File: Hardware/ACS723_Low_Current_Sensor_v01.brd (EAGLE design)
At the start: 31.8 x 15.2 mm, 26 parts, among them U1 ACS723, U2 OPA344

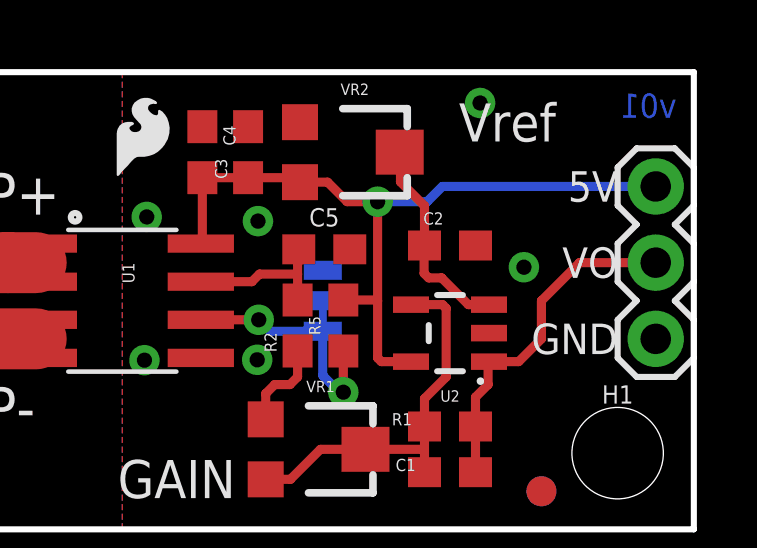
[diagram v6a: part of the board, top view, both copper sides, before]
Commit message: Adjusted the position of a cap
-C2  Y-axis -.05"
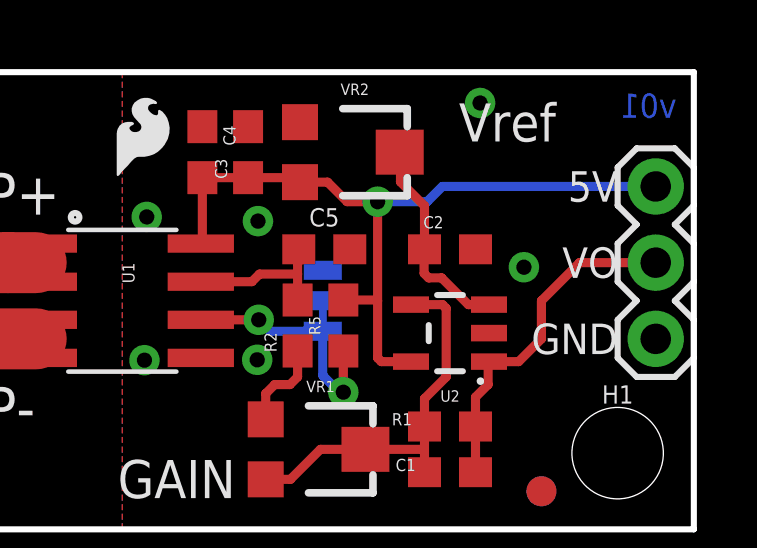
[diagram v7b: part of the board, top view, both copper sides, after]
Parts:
- moved C2 0.13 mm to (23.6, 9.33)
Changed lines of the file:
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@@
 <attribute name="PROD_ID" value="CAP-07883" x="23.622" y="1.905" size="1.778" layer="27" rot="R180" display="off"/>
 </element>
-<element name="C2" library="SparkFun-Capacitors" package="0603" value="0.1uF" x="23.622" y="9.4615" smashed="yes">
-<attribute name="NAME" x="22.733" y="10.16" size="0.4064" layer="25"/>
-<attribute name="VALUE" value="0.1uF" x="23.0505" y="10.0965" size="0.4064" layer="27"/>
-<attribute name="PROD_ID" value="CAP-00810" x="23.622" y="9.4615" size="1.778" layer="27" display="off"/>
+<element name="C2" library="SparkFun-Capacitors" package="0603" value="0.1uF" x="23.622" y="9.3345" smashed="yes">
+<attribute name="NAME" x="22.733" y="10.033" size="0.4064" layer="25"/>
+<attribute name="VALUE" value="0.1uF" x="23.0505" y="9.9695" size="0.4064" layer="27"/>
+<attribute name="PROD_ID" value="CAP-00810" x="23.622" y="9.3345" size="1.778" layer="27" display="off"/>
 </element>
 <element name="C3" library="SparkFun-Capacitors" package="0603" value="0.1uF" x="16.891" y="12.573" smashed="yes" rot="R90">
@@
 <wire x1="22.9108" y1="8.382" x2="22.7584" y2="8.5344" width="0.3048" layer="1"/>
 <wire x1="22.7584" y1="8.5344" x2="22.7584" y2="9.4479" width="0.3048" layer="1"/>
-<wire x1="22.7584" y1="9.4479" x2="22.772" y2="9.4615" width="0.3048" layer="1"/>
-<wire x1="22.772" y1="9.4615" x2="22.772" y2="10.7814" width="0.3048" layer="1"/>
+<wire x1="22.7584" y1="9.4479" x2="22.772" y2="9.3345" width="0.3048" layer="1"/>
+<wire x1="22.772" y1="9.3345" x2="22.772" y2="10.7814" width="0.3048" layer="1"/>
 <wire x1="22.772" y1="10.7814" x2="21.971" y2="11.5824" width="0.3048" layer="1"/>
 <wire x1="21.971" y1="11.5824" x2="21.971" y2="12.549" width="0.3048" layer="1"/>
